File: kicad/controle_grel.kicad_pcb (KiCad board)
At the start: 2 copper layers, 50 x 30 mm, 17 parts, among them J1 ESP01, J2 Barrel_Jack_Switch, Q1 BC337, U1 AMS1117-3.3

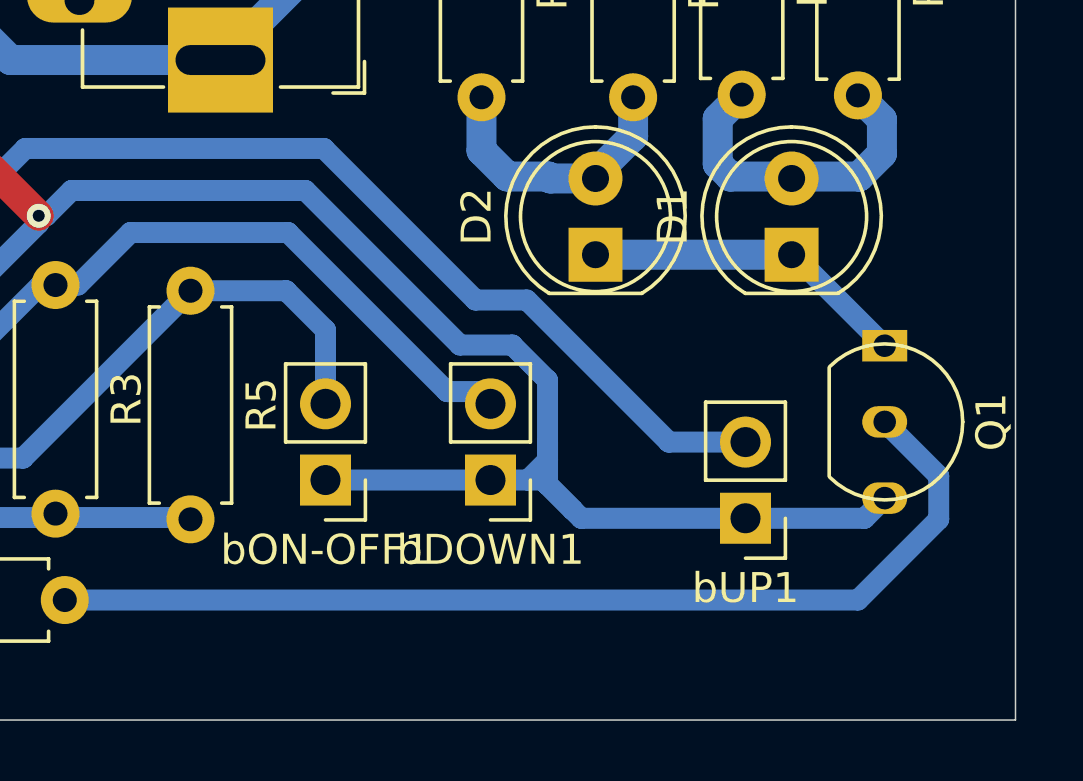
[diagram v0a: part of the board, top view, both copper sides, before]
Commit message: pcb: corrijindo pinagem esp01 e aumentando espaçamento
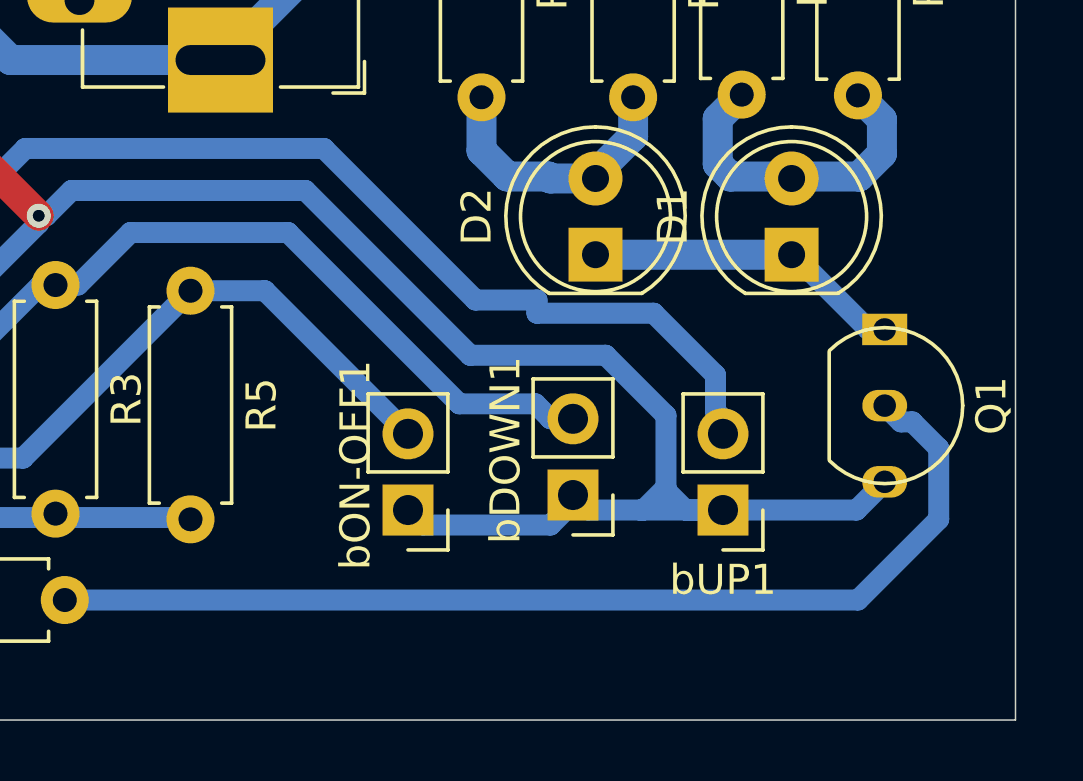
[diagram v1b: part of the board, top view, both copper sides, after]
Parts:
- moved bON-OFF1 2.93 mm to (110.2, 72.0)
- moved bDOWN1 2.80 mm to (115.8, 71.5)
- moved bUP1 0.80 mm to (120.8, 72.0)
- moved Q1 0.54 mm to (126.1, 67.2)
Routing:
- net B_DOWN: track 30.0 -> 32.9 mm
- net B_ON-OFF: track 25.3 -> 27.1 mm
- net GND: track 100.0 -> 101.6 mm
- net Net-(Q1-B): track 34.2 -> 35.0 mm

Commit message: pcb: corrigido lado do ams1117 (colocando no botton)
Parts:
- U1: moved to B.Cu
- moved U1 2.69 mm to (91.0, 55.0), turned to 90 degrees
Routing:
- net GND: track 101.6 -> 78.3 mm, vias 3 -> 2
- net CHIP_EN: track 50.8 -> 58.2 mm, vias 1 -> 0
- net +5V: track 37.7 -> 42.7 mm, vias 1 -> 0

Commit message: Consegui corroer a plaquinhaaaa
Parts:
- removed J2: Barrel_Jack_Switch, Connector_BarrelJack:BarrelJack_Horizontal
- J1: footprint Connector_PinSocket_2.54mm:PinSocket_2x04_P2.54mm_Vertical -> Connector_PinSocket_2.54mm:PinSocket_2x04_P2.54mm_Vertical_SMD
- Q1: footprint Package_TO_SOT_THT:TO-92_Inline -> Connector_PinHeader_2.54mm:PinHeader_1x03_P2.54mm_Horizontal
- R1, R2, R3, R4, R5, R6, R7, R8: footprint Resistor_THT:R_Axial_DIN0207_L6.3mm_D2.5mm_P7.62mm_Horizontal -> Resistor_SMD:R_1206_3216Metric
- U1: moved to F.Cu
- moved U1 54.9 mm to (145.9, 55.0)
- moved R1 51.2 mm to (141.2, 48.3), turned to 135 degrees
- moved J1 50.4 mm to (137.1, 55.5), turned to 90 degrees
- moved bON-OFF1 46.3 mm to (145.7, 42.2), turned to -90 degrees
- moved bDOWN1 45.5 mm to (145.8, 37.3), turned to -90 degrees
- moved R2 44.4 mm to (134.4, 64.9), turned to -90 degrees
- moved R3 42.4 mm to (133.3, 40.4), turned to 135 degrees
- moved R5 39.9 mm to (137.3, 44.2), turned to 135 degrees
- moved bUP1 34.4 mm to (145.9, 48.5), turned to -90 degrees
- moved R7 31.9 mm to (140.6, 66.1)
- moved D2 27.9 mm to (142.6, 73.4)
- moved R6 27.4 mm to (143.9, 66.1)
- moved R4 27.0 mm to (147.3, 66.1)
- moved R8 24.9 mm to (137.3, 66.1)
- moved D1 17.6 mm to (137.6, 73.4)
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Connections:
- D2 pad 2: Net-(D2-A) -> Net-(D1-A)
- J1 pad 2: B_UP -> IR
- J1 pad 7: IR -> B_UP
- R1 pad 2: CHIP_EN -> GND
- R3 pad 2: CHIP_EN -> GND
- R5 pad 2: CHIP_EN -> GND
- R7 pad 2: Net-(D2-A) -> Net-(D1-A)
- R8 pad 2: Net-(D2-A) -> Net-(D1-A)
- bDOWN1 pad 1: GND -> CHIP_EN
- bON-OFF1 pad 1: GND -> CHIP_EN
- bUP1 pad 1: GND -> CHIP_EN
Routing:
- net B_UP: track 44.5 -> 5.49 mm
- net Net-(Q1-B): track 35.0 -> 3.51 mm
- net GND: track 78.3 -> 50.4 mm, vias 2 -> 5
- net +5V: track 42.7 -> 16.8 mm
- net CHIP_EN: track 58.2 -> 38.8 mm
- net Net-(D1-A): track 10.9 -> 25.9 mm
- net B_ON-OFF: track 27.1 -> 14.1 mm
- net Net-(D2-A): track 9.19 -> 0.00 mm
- net B_DOWN: track 32.9 -> 26.5 mm
- net Net-(D1-K): track 10.7 -> 13.4 mm
- net IR: track 3.99 -> 5.87 mm
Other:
- board outline removed
